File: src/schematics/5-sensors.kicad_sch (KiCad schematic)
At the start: 33 parts, among them Q501 NX6008NBKW, Q502 NX6008NBKW, Q503 NX6008NBKW, Q504 NX6008NBKW, Q505 NX6008NBKW, U501 TPS7A2028PDBVR, U502 DPS310XTSA1, U503 HDC3022, U504 VL6180V1NR1

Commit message: Further elaboration of the circuitry surrounding the microcontroller.  Plus a few typos / tidy-ups.
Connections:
- net PRX_GPIO0: now also R508.2
- net PRX_GPIO1: no longer R508.2
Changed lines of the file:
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@@
   (junction (at 154.94 139.7) (diameter 0) (color 0 0 0 0)
   )
+  (junction (at 134.62 213.36) (diameter 0) (color 0 0 0 0)
+  )
   (junction (at 266.7 99.06) (diameter 0) (color 0 0 0 0)
   )
@@
   (junction (at 208.28 43.18) (diameter 0) (color 0 0 0 0)
   )
-  (junction (at 134.62 223.52) (diameter 0) (color 0 0 0 0)
-  )
   (junction (at 223.52 195.58) (diameter 0) (color 0 0 0 0)
   )
@@
     (stroke (width 0) (type default))
   )
+  (wire (pts (xy 134.62 213.36) (xy 180.34 213.36))
+    (stroke (width 0) (type default))
+  )
   (wire (pts (xy 228.6 81.28) (xy 241.3 81.28))
     (stroke (width 0) (type default))
   )
-  (wire (pts (xy 114.3 213.36) (xy 180.34 213.36))
+  (wire (pts (xy 114.3 213.36) (xy 134.62 213.36))
     (stroke (width 0) (type default))
   )
@@
     (stroke (width 0) (type default))
   )
-  (wire (pts (xy 134.62 223.52) (xy 147.32 223.52))
+  (wire (pts (xy 114.3 223.52) (xy 147.32 223.52))
     (stroke (width 0) (type default))
   )
@@
     (stroke (width 0) (type default))
   )
-  (wire (pts (xy 114.3 223.52) (xy 134.62 223.52))
-    (stroke (width 0) (type default))
-  )
   (wire (pts (xy 284.48 195.58) (xy 271.78 195.58))
     (stroke (width 0) (type default))
@@
     (stroke (width 0) (type default))
   )
-  (wire (pts (xy 134.62 208.28) (xy 134.62 223.52))
-    (stroke (width 0) (type default))
-  )
+  (wire (pts (xy 134.62 208.28) (xy 134.62 213.36))
+    (stroke (width 0) (type default))
+  )

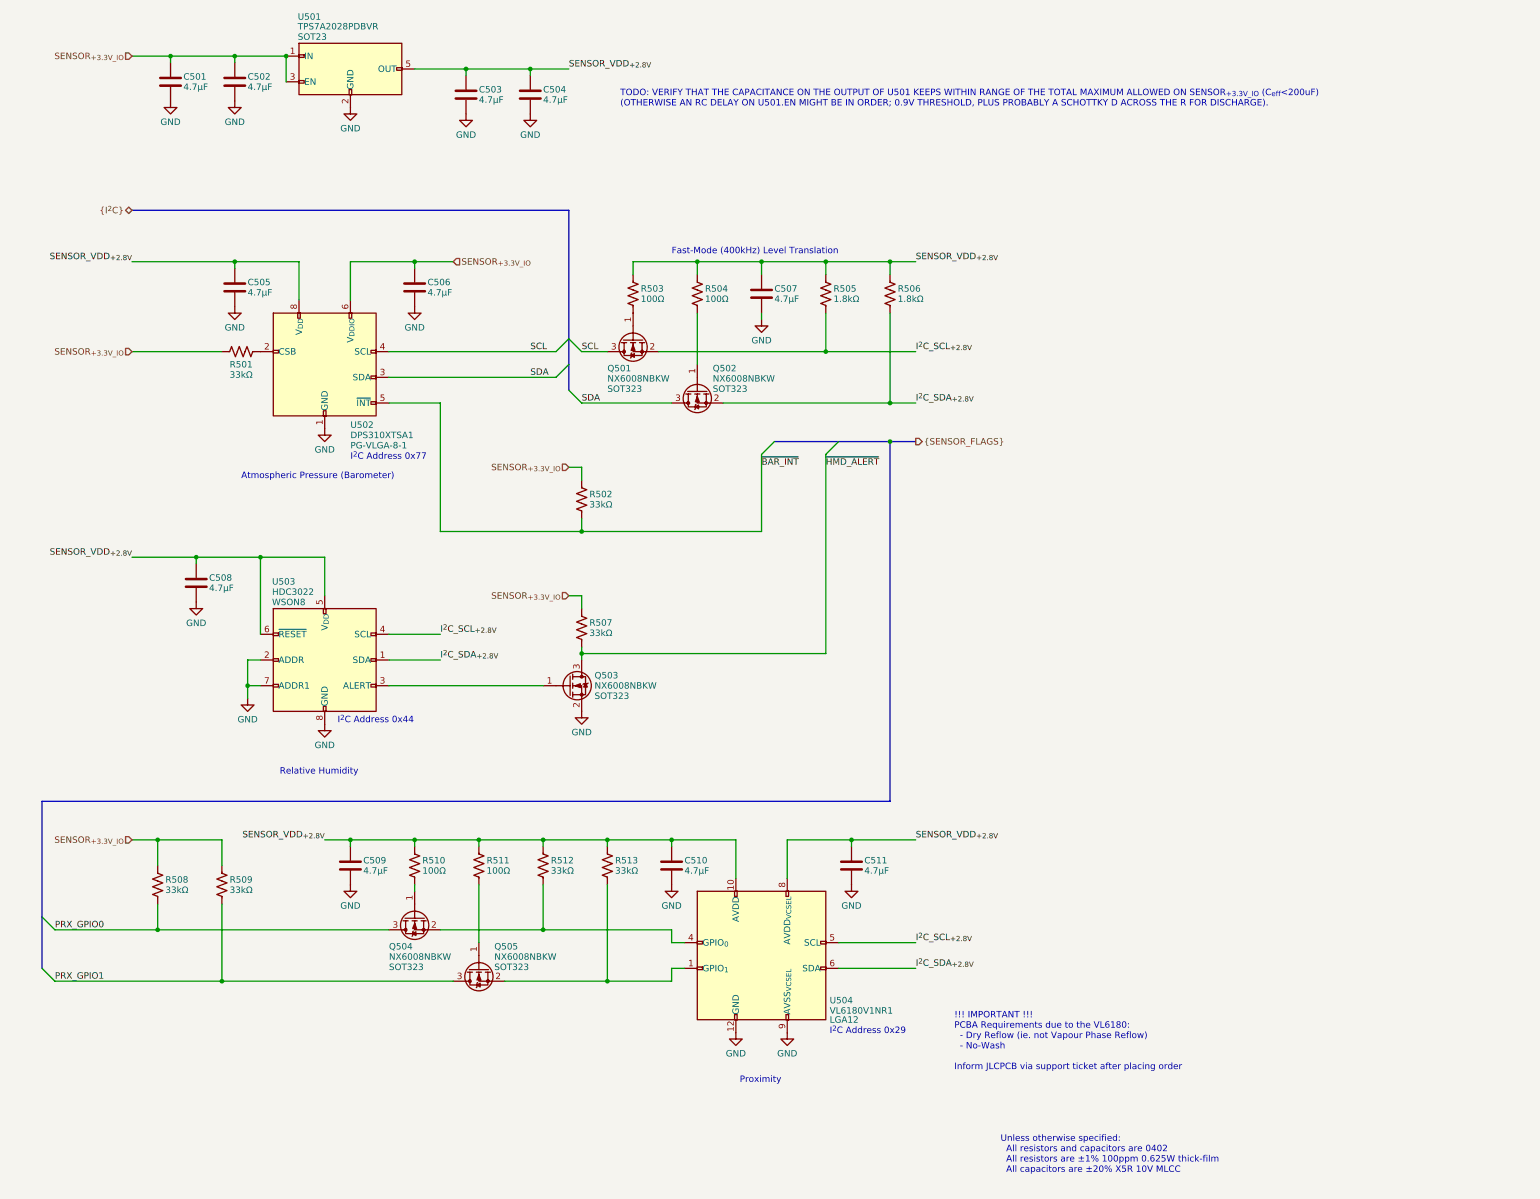
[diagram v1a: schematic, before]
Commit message: Various tidy-ups and checks, mainly around the bypass capacitors.  Added a load of test points.
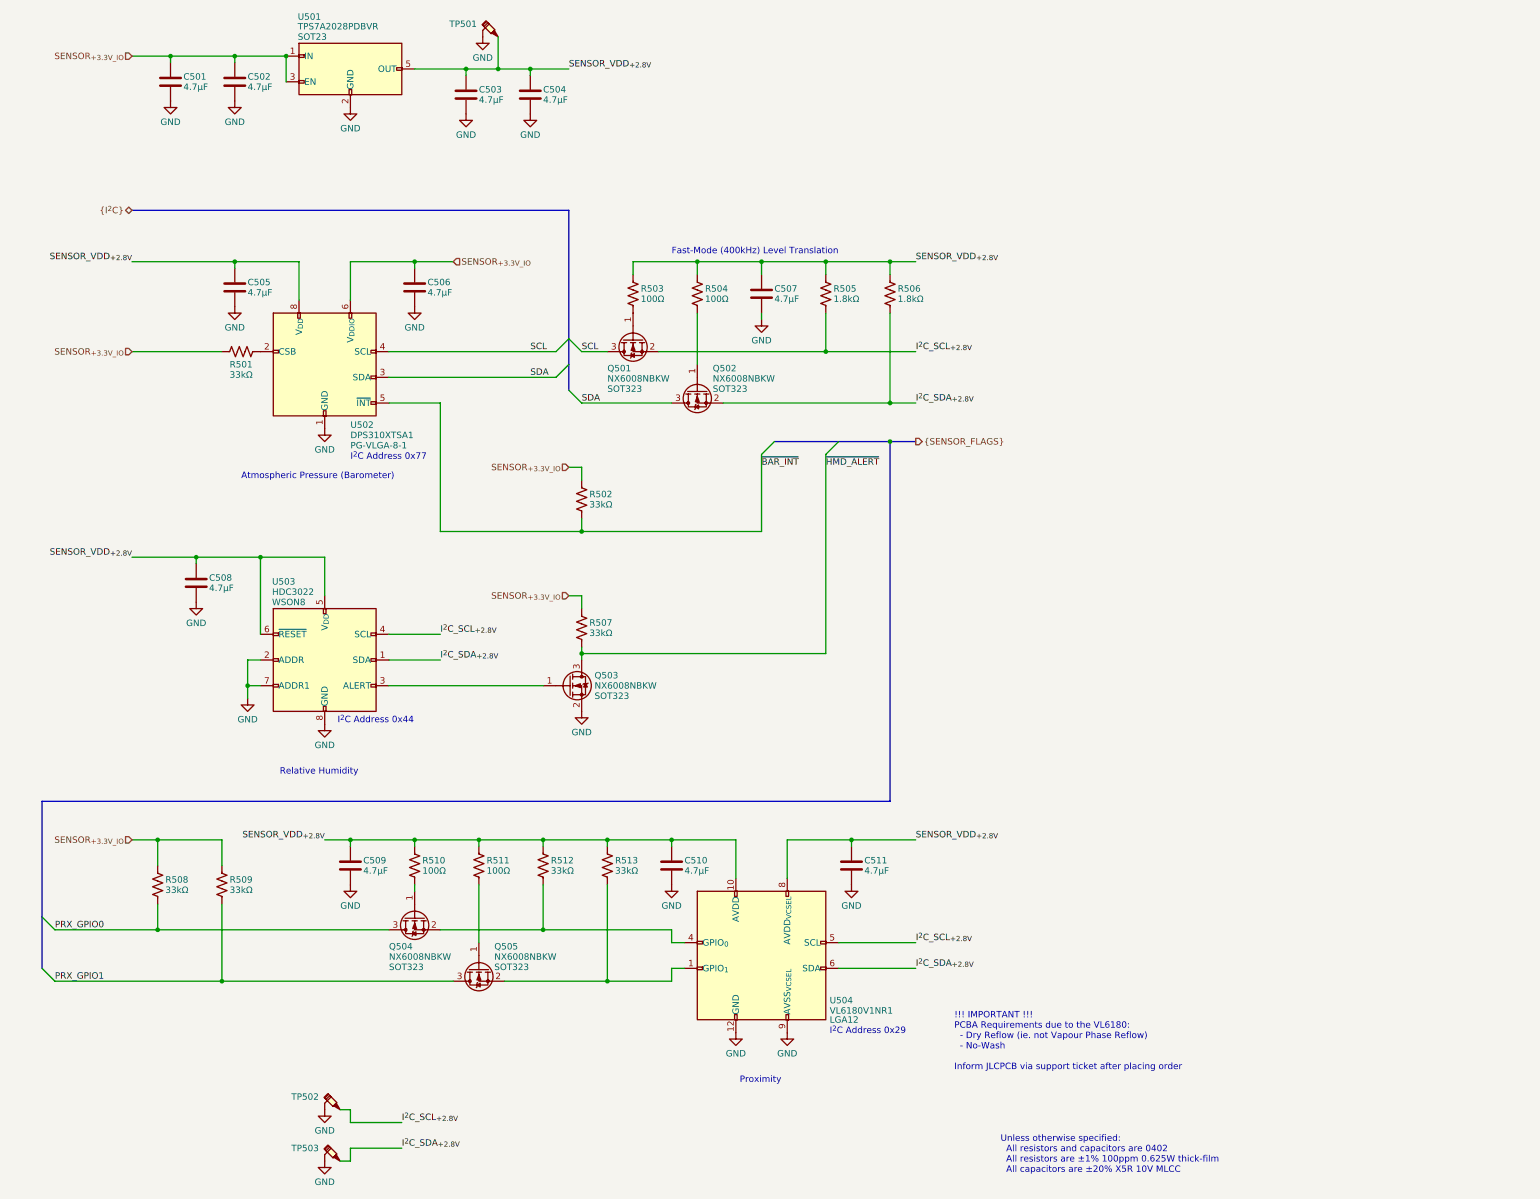
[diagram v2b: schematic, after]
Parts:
- added TP501, TP502, TP503: ~, restall-generic-test:testpoint-SP3050A-with-short-gnd, symbol restall-generic-test:testpoint-probe-with-gnd
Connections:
- net GND: now also TP501.2 (GND), TP502.2 (GND), TP503.2 (GND)
- net I^{2}C_SCL_{+2.8V}: now also TP502.1
- net I^{2}C_SDA_{+2.8V}: now also TP503.1
- net SENSOR_VDD_{+2.8V}: now also TP501.1
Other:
- note removed: "TODO: VERIFY THAT THE CAPACITANCE ON THE OUTPUT OF U501 KEEPS WITHIN RANGE OF THE TOTAL MAXIMUM ALLOWED ON SENSOR_{+3.3V_IO} (C_{eff}<200uF) (OTHERWISE AN RC DELAY ON U501.EN MIGHT BE IN ORDER; 0.9V THRESHOLD, PLUS PROBABLY A SCHOTTKY D ACROSS THE R FOR DISCHARGE)."
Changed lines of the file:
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@@
   (junction (at 142.24 139.7) (diameter 0) (color 0 0 0 0)
   )
+  (junction (at 201.93 43.18) (diameter 0) (color 0 0 0 0)
+  )
   (junction (at 134.62 195.58) (diameter 0) (color 0 0 0 0)
   )
@@
     (stroke (width 0) (type default))
   )
+  (wire (pts (xy 201.93 43.18) (xy 208.28 43.18))
+    (stroke (width 0) (type default))
+  )
   (wire (pts (xy 180.34 109.22) (xy 190.5 109.22))
     (stroke (width 0) (type default))
@@
     (stroke (width 0) (type default))
   )
+  (wire (pts (xy 201.93 36.83) (xy 201.93 43.18))
+    (stroke (width 0) (type default))
+  )
   (wire (pts (xy 279.4 81.28) (xy 284.48 81.28))
     (stroke (width 0) (type default))
@@
     (stroke (width 0) (type default))
   )
+  (wire (pts (xy 172.72 251.46) (xy 172.72 248.92))
+    (stroke (width 0) (type default))
+  )
+  (wire (pts (xy 172.72 251.46) (xy 182.88 251.46))
+    (stroke (width 0) (type default))
+  )
   (wire (pts (xy 185.42 81.28) (xy 185.42 82.55))
     (stroke (width 0) (type default))
@@
     (stroke (width 0) (type default))
   )
+  (wire (pts (xy 172.72 256.54) (xy 172.72 259.08))
+    (stroke (width 0) (type default))
+  )
   (wire (pts (xy 203.2 223.52) (xy 223.52 223.52))
     (stroke (width 0) (type default))
@@
     (stroke (width 0) (type default))
   )
-  (wire (pts (xy 195.58 43.18) (xy 208.28 43.18))
+  (wire (pts (xy 195.58 43.18) (xy 201.93 43.18))
+    (stroke (width 0) (type default))
+  )
+  (wire (pts (xy 172.72 259.08) (xy 170.688 259.08))
     (stroke (width 0) (type default))
   )
@@
     (stroke (width 0) (type default))
   )
+  (wire (pts (xy 172.72 256.54) (xy 182.88 256.54))
+    (stroke (width 0) (type default))
+  )
   (wire (pts (xy 142.24 139.7) (xy 154.94 139.7))
     (stroke (width 0) (type default))
@@
   )
   (wire (pts (xy 279.4 81.28) (xy 279.4 83.82))
+    (stroke (width 0) (type default))
+  )
+  (wire (pts (xy 172.72 248.92) (xy 170.688 248.92))
     (stroke (width 0) (type default))
   )
@@
     (effects (font (size 1.27 1.27)) (justify left bottom))
   )
-  (text "TODO: VERIFY THAT THE CAPACITANCE ON THE OUTPUT OF U501 KEEPS WITHIN RANGE OF THE TOTAL MAXIMUM ALLOWED ON SENSOR_{+3.3V_IO} (C_{eff}<200uF)\n(OTHERWISE AN RC DELAY ON U501.EN MIGHT BE IN ORDER; 0.9V THRESHOLD, PLUS PROBABLY A SCHOTTKY D ACROSS THE R FOR DISCHARGE)."
-    (at 226.06 50.8 0)
-    (effects (font (size 1.27 1.27)) (justify left bottom))
-  )
   (text "Atmospheric Pressure (Barometer)" (at 151.13 124.46 0)
     (effects (font (size 1.27 1.27)) (justify left bottom))
@@
     (effects (font (size 1.27 1.27)) (justify right bottom))
   )
+  (label "I^{2}C_SCL_{+2.8V}" (at 182.88 251.46 0) (fields_autoplaced)
+    (effects (font (size 1.27 1.27)) (justify left bottom))
+  )
   (label "I^{2}C_SCL_{+2.8V}" (at 284.48 215.9 0) (fields_autoplaced)
     (effects (font (size 1.27 1.27)) (justify left bottom))
@@
     (effects (font (size 1.27 1.27)) (justify left bottom))
   )
+  (label "I^{2}C_SDA_{+2.8V}" (at 182.88 256.54 0) (fields_autoplaced)
+    (effects (font (size 1.27 1.27)) (justify left bottom))
+  )
   (label "SCL" (at 208.28 99.06 0) (fields_autoplaced)
     (effects (font (size 1.27 1.27)) (justify left bottom))
@@
         (path "/56d623d3-22db-4d43-a9d9-e6bb4bb68946/f496ae57-4ed4-47d4-8c97-f77f6741aea7"
           (reference "R503") (unit 1)
+        )
+      )
+    )
+  )
+  (symbol (lib_id "restall-generic-power:GND") (at 167.64 248.92 0) (unit 1)
+    (in_bom yes) (on_board yes) (dnp no) (fields_autoplaced)
+    (property "Reference" "#PWR0261" (at 167.64 255.27 0)
+      (effects (font (size 1.27 1.27)) hide)
+    )
+    (property "Value" "GND" (at 167.64 253.0531 0)
+      (effects (font (size 1.27 1.27)))
+    )
+    (property "Footprint" "" (at 167.64 248.92 0)
+      (effects (font (size 1.27 1.27)) hide)
+    )
+    (property "Datasheet" "" (at 167.64 248.92 0)
+      (effects (font (size 1.27 1.27)) hide)
+    )
+    (pin "1")
+    (instances
+      (project "msf-owl-clock"
+        (path "/56d623d3-22db-4d43-a9d9-e6bb4bb68946/f496ae57-4ed4-47d4-8c97-f77f6741aea7"
+          (reference "#PWR0261") (unit 1)
         )
       )
@@
         (path "/56d623d3-22db-4d43-a9d9-e6bb4bb68946/f496ae57-4ed4-47d4-8c97-f77f6741aea7"
           (reference "C507") (unit 1)
+        )
+      )
+    )
+  )
+  (symbol (lib_id "restall-generic-test:testpoint-probe-with-gnd") (at 170.688 259.08 0) (mirror y) (unit 1)
+    (in_bom no) (on_board yes) (dnp no)
+    (property "Reference" "TP503" (at 161.036 256.54 0)
+      (effects (font (size 1.27 1.27)) (justify right))
+    )
+    (property "Value" "~" (at 169.037 255.016 0)
+      (effects (font (size 1.27 1.27)) (justify right) hide)
+    )
+    (property "Footprint" "restall-generic-test:testpoint-SP3050A-with-short-gnd" (at 165.608 259.08 0)
+      (effects (font (size 1.27 1.27)) (justify right) hide)
+    )
+    (property "Datasheet" "~" (at 165.608 259.08 0)
+      (effects (font (size 1.27 1.27)) (justify right) hide)
+    )
+    (pin "2")
+    (pin "1")
+    (instances
+      (project "msf-owl-clock"
+        (path "/56d623d3-22db-4d43-a9d9-e6bb4bb68946/f496ae57-4ed4-47d4-8c97-f77f6741aea7"
+          (reference "TP503") (unit 1)
         )
       )
@@
     )
   )
+  (symbol (lib_id "restall-generic-power:GND") (at 198.882 36.83 0) (unit 1)
+    (in_bom yes) (on_board yes) (dnp no) (fields_autoplaced)
+    (property "Reference" "#PWR0266" (at 198.882 43.18 0)
+      (effects (font (size 1.27 1.27)) hide)
+    )
+    (property "Value" "GND" (at 198.882 40.9631 0)
+      (effects (font (size 1.27 1.27)))
+    )
+    (property "Footprint" "" (at 198.882 36.83 0)
+      (effects (font (size 1.27 1.27)) hide)
+    )
+    (property "Datasheet" "" (at 198.882 36.83 0)
+      (effects (font (size 1.27 1.27)) hide)
+    )
+    (pin "1")
+    (instances
+      (project "msf-owl-clock"
+        (path "/56d623d3-22db-4d43-a9d9-e6bb4bb68946/f496ae57-4ed4-47d4-8c97-f77f6741aea7"
+          (reference "#PWR0266") (unit 1)
+        )
+      )
+    )
+  )
   (symbol (lib_id "restall-generic-power:GND") (at 167.64 114.3 0) (unit 1)
     (in_bom yes) (on_board yes) (dnp no) (fields_autoplaced)
@@
     )
   )
+  (symbol (lib_id "restall-generic-test:testpoint-probe-with-gnd") (at 170.688 248.92 0) (mirror y) (unit 1)
+    (in_bom no) (on_board yes) (dnp no)
+    (property "Reference" "TP502" (at 161.036 246.38 0)
+      (effects (font (size 1.27 1.27)) (justify right))
+    )
+    (property "Value" "~" (at 169.037 244.856 0)
+      (effects (font (size 1.27 1.27)) (justify right) hide)
+    )
+    (property "Footprint" "restall-generic-test:testpoint-SP3050A-with-short-gnd" (at 165.608 248.92 0)
+      (effects (font (size 1.27 1.27)) (justify right) hide)
+    )
+    (property "Datasheet" "~" (at 165.608 248.92 0)
+      (effects (font (size 1.27 1.27)) (justify right) hide)
+    )
+    (pin "2")
+    (pin "1")
+    (instances
+      (project "msf-owl-clock"
+        (path "/56d623d3-22db-4d43-a9d9-e6bb4bb68946/f496ae57-4ed4-47d4-8c97-f77f6741aea7"
+          (reference "TP502") (unit 1)
+        )
+      )
+    )
+  )
   (symbol (lib_id "restall-generic-capacitors:capacitor-unpolarised") (at 208.28 48.26 0) (unit 1)
     (in_bom yes) (on_board yes) (dnp no)
@@
         (path "/56d623d3-22db-4d43-a9d9-e6bb4bb68946/f496ae57-4ed4-47d4-8c97-f77f6741aea7"
           (reference "R512") (unit 1)
+        )
+      )
+    )
+  )
+  (symbol (lib_id "restall-generic-test:testpoint-probe-with-gnd") (at 201.93 36.83 0) (mirror y) (unit 1)
+    (in_bom no) (on_board yes) (dnp no)
+    (property "Reference" "TP501" (at 192.278 34.29 0)
+      (effects (font (size 1.27 1.27)) (justify right))
+    )
+    (property "Value" "~" (at 200.279 32.766 0)
+      (effects (font (size 1.27 1.27)) (justify right) hide)
+    )
+    (property "Footprint" "restall-generic-test:testpoint-SP3050A-with-short-gnd" (at 196.85 36.83 0)
+      (effects (font (size 1.27 1.27)) (justify right) hide)
+    )
+    (property "Datasheet" "~" (at 196.85 36.83 0)
+      (effects (font (size 1.27 1.27)) (justify right) hide)
+    )
+    (pin "2")
+    (pin "1")
+    (instances
+      (project "msf-owl-clock"
+        (path "/56d623d3-22db-4d43-a9d9-e6bb4bb68946/f496ae57-4ed4-47d4-8c97-f77f6741aea7"
+          (reference "TP501") (unit 1)
         )
       )
@@
         )
       )
+    )
+  )
+  (symbol (lib_id "restall-generic-power:GND") (at 167.64 259.08 0) (unit 1)
+    (in_bom yes) (on_board yes) (dnp no) (fields_autoplaced)
+    (property "Reference" "#PWR0262" (at 167.64 265.43 0)
+      (effects (font (size 1.27 1.27)) hide)
+    )
+    (property "Value" "GND" (at 167.64 263.2131 0)
+      (effects (font (size 1.27 1.27)))
+    )
+    (property "Footprint" "" (at 167.64 259.08 0)
+      (effects (font (size 1.27 1.27)) hide)
+    )
+    (property "Datasheet" "" (at 167.64 259.08 0)
+      (effects (font (size 1.27 1.27)) hide)
+    )
+    (pin "1")
+    (instances
+      (project "msf-owl-clock"
+        (path "/56d623d3-22db-4d43-a9d9-e6bb4bb68946/f496ae57-4ed4-47d4-8c97-f77f6741aea7"
+          (reference "#PWR0262") (unit 1)
+        )
+      )

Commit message: Finalised various components and footprints.  Various tidy-ups.
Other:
- title: MSF Owl Clock - Environmental Sensors -> MSF Owl Clock - Environmental Sensors Module
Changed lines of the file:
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@@
   (paper "A3")
   (title_block
-    (title "MSF Owl Clock - Environmental Sensors")
+    (title "MSF Owl Clock - Environmental Sensors Module")
     (rev "0.1")
     (company "Pete Restall <pete@restall.net>")

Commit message: Added part numbers for the capacitors.
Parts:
- C501, C502, C503, C504, C505, C506, C507, C508, C509, C510, C511: ManufacturerPartNumber (none) -> CL05A475MP5NRNC
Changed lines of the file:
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@@
       (effects (font (size 1.27 1.27)) (justify left) hide)
     )
-    (property "ManufacturerPartNumber" "" (at 185.42 86.36 0)
+    (property "ManufacturerPartNumber" "CL05A475MP5NRNC" (at 185.42 86.36 0)
       (effects (font (size 1.27 1.27)) (justify left) hide)
     )
@@
       (effects (font (size 1.27 1.27)) (justify left) hide)
     )
-    (property "ManufacturerPartNumber" "" (at 142.24 144.78 0)
+    (property "ManufacturerPartNumber" "CL05A475MP5NRNC" (at 142.24 144.78 0)
       (effects (font (size 1.27 1.27)) (justify left) hide)
     )
@@
       (effects (font (size 1.27 1.27)) (justify left) hide)
     )
-    (property "ManufacturerPartNumber" "" (at 254 87.63 0)
+    (property "ManufacturerPartNumber" "CL05A475MP5NRNC" (at 254 87.63 0)
       (effects (font (size 1.27 1.27)) (justify left) hide)
     )
@@
       (effects (font (size 1.27 1.27)) (justify left) hide)
     )
-    (property "ManufacturerPartNumber" "" (at 137.16 45.72 0)
+    (property "ManufacturerPartNumber" "CL05A475MP5NRNC" (at 137.16 45.72 0)
       (effects (font (size 1.27 1.27)) (justify left) hide)
     )
@@
       (effects (font (size 1.27 1.27)) (justify left) hide)
     )
-    (property "ManufacturerPartNumber" "" (at 271.78 200.66 0)
+    (property "ManufacturerPartNumber" "CL05A475MP5NRNC" (at 271.78 200.66 0)
       (effects (font (size 1.27 1.27)) (justify left) hide)
     )
@@
       (effects (font (size 1.27 1.27)) (justify left) hide)
     )
-    (property "ManufacturerPartNumber" "" (at 195.58 48.26 0)
+    (property "ManufacturerPartNumber" "CL05A475MP5NRNC" (at 195.58 48.26 0)
       (effects (font (size 1.27 1.27)) (justify left) hide)
     )
@@
       (effects (font (size 1.27 1.27)) (justify left) hide)
     )
-    (property "ManufacturerPartNumber" "" (at 149.86 86.36 0)
+    (property "ManufacturerPartNumber" "CL05A475MP5NRNC" (at 149.86 86.36 0)
       (effects (font (size 1.27 1.27)) (justify left) hide)
     )
@@
       (effects (font (size 1.27 1.27)) (justify left) hide)
     )
-    (property "ManufacturerPartNumber" "" (at 208.28 48.26 0)
+    (property "ManufacturerPartNumber" "CL05A475MP5NRNC" (at 208.28 48.26 0)
       (effects (font (size 1.27 1.27)) (justify left) hide)
     )
@@
       (effects (font (size 1.27 1.27)) (justify left) hide)
     )
-    (property "ManufacturerPartNumber" "" (at 149.86 45.72 0)
+    (property "ManufacturerPartNumber" "CL05A475MP5NRNC" (at 149.86 45.72 0)
       (effects (font (size 1.27 1.27)) (justify left) hide)
     )
@@
       (effects (font (size 1.27 1.27)) (justify left) hide)
     )
-    (property "ManufacturerPartNumber" "" (at 236.22 200.66 0)
+    (property "ManufacturerPartNumber" "CL05A475MP5NRNC" (at 236.22 200.66 0)
       (effects (font (size 1.27 1.27)) (justify left) hide)
     )
@@
       (effects (font (size 1.27 1.27)) (justify left) hide)
     )
-    (property "ManufacturerPartNumber" "" (at 172.72 200.66 0)
-      (effects (font (size 1.27 1.27)) (justify left) hide)
-    )
+    (property "ManufacturerPartNumber" "CL05A475MP5NRNC" (at 172.72 200.66 0)
+      (effects (font (size 1.27 1.27)) (justify left) hide)
+    )
